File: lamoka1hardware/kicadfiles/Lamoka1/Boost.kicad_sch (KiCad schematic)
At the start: 38 parts, among them Q4 NMOS

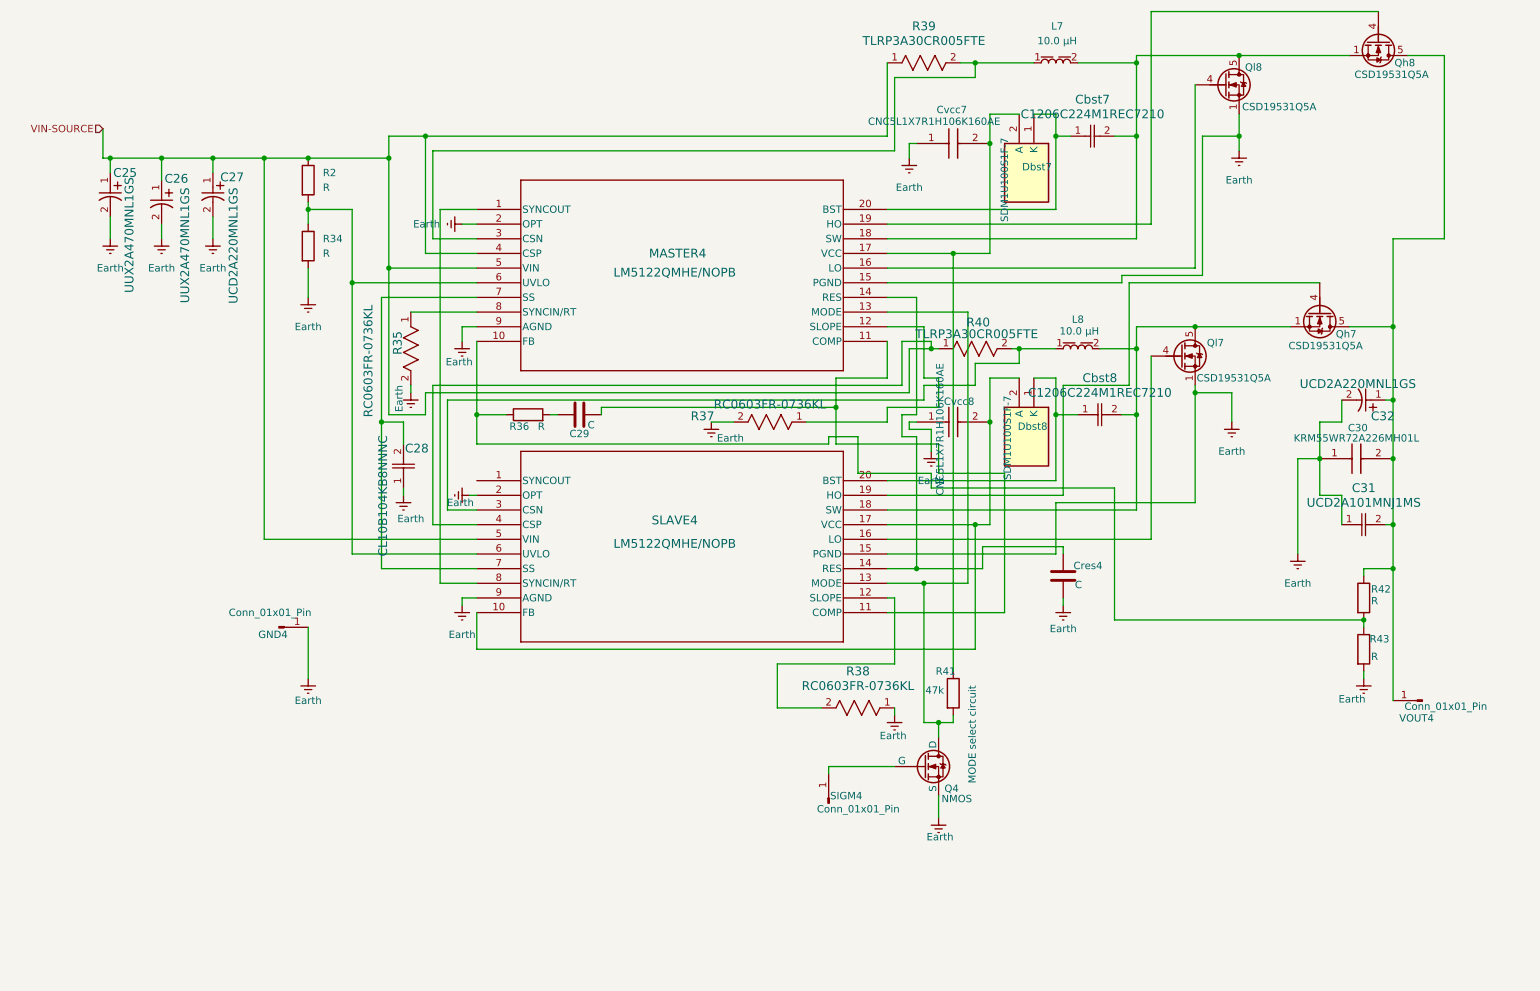
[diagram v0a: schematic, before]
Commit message: ADD the schematic for testing the boost section is all done and configured
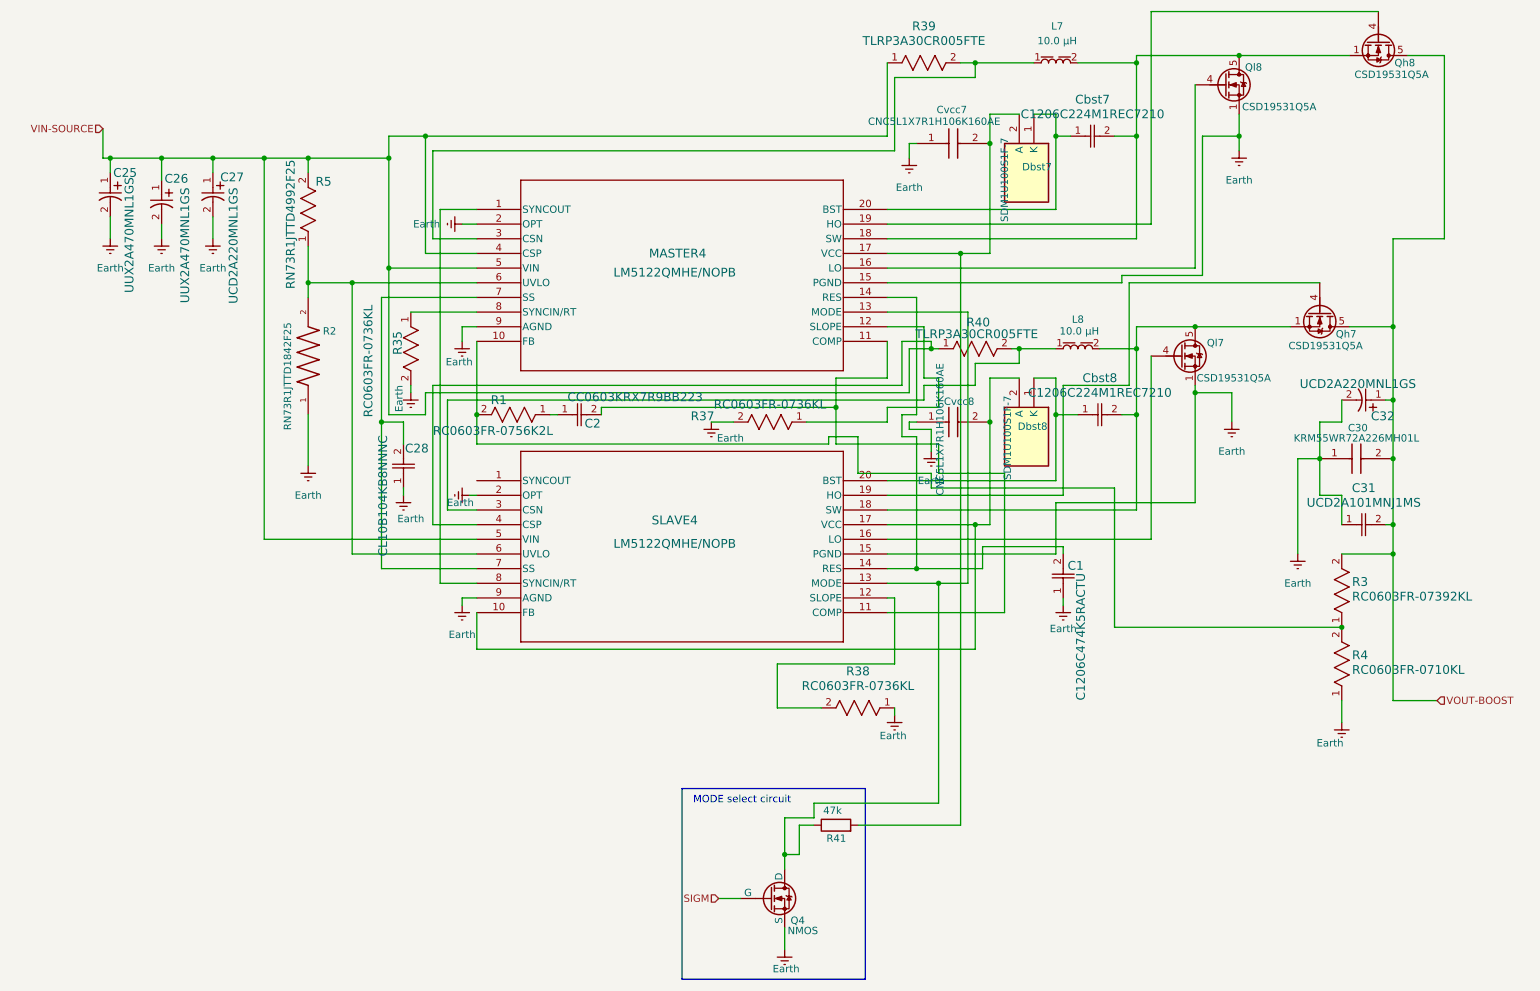
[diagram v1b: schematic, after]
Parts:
- removed C29, Cres4: C, symbol Device:C
- removed GND4, SIGM4, VOUT4: Conn_01x01_Pin, symbol Connector:Conn_01x01_Pin
- removed R2, R34, R36, R42, R43: R, symbol Device:R
- added C1: C1206C474K5RACTU, Components:CAPC340180_100N_KEM, symbol 2026-06-26_00-29-12:C1206C474K5RACTU
- added C2: CC0603KRX7R9BB223, Components:YAG_CC0603_YAG, symbol 2026-06-26_01-22-08:CC0603KRX7R9BB223
- added R1: RC0603FR-0756K2L, Components:RC0603N_YAG, symbol 2026-06-26_01-14-22:RC0603FR-0756K2L
- added R2: RN73R1JTTD1842F25, Components:RESC1608X55N, symbol RN73R1JTTD1842F25:RN73R1JTTD1842F25
- added R3: RC0603FR-07392KL, Components:RC0603N_YAG, symbol 2026-06-26_11-23-01:RC0603FR-07392KL
- added R4: RC0603FR-0710KL, Components:RC0603N_YAG, symbol 2026-06-26_11-27-26:RC0603FR-0710KL
- added R5: RN73R1JTTD4992F25, Components:RES_RN73R_1J_KOA, symbol 2026-06-26_12-12-49:RN73R1JTTD4992F25
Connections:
- net Earth: now also C1.1, R2.1, R4.1
- net VIN-SOURCE: now also R5.2
- net at Cvcc7.2, Dbst7.2 (A), MASTER4.17 (VCC): now also R41.2; no longer R41.1
- net at MASTER4.13 (MODE), Q4.1 (D), SLAVE4.13 (MODE): now also R41.1; no longer R41.2
- net VOUT-BOOST: now reaches C30.2, C31.2, C32.1, Qh7.5 (D), Qh8.5 (D)
- net VOUT-BOOST: now also R3.2
- net at MASTER4.14 (RES), SLAVE4.14 (RES): now also C1.2
- net SIGM: now reaches Q4.2 (G)
- net at MASTER4.10 (FB): now also R1.2, R3.1, R4.2
- net at MASTER4.6 (UVLO), SLAVE4.6 (UVLO): now also R2.2, R5.1
- net at MASTER4.11 (COMP), SLAVE4.11 (COMP): now also C2.2
- new net: C2.1, R1.1
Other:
- moved on the sheet: Q4
